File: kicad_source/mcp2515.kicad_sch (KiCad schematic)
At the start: 14 parts, among them CN4 SM04B-GHS-TB, CN5 SM04B-GHS-TB, U8 MCP2515T-I/SO, U9 SN65HVD232, Y1 X322516MLB4SI

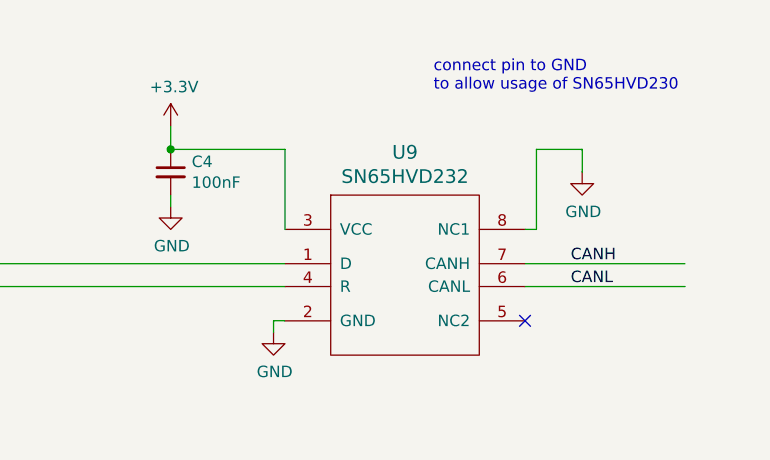
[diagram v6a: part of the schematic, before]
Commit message: switched to JLCPCB basic parts where possible
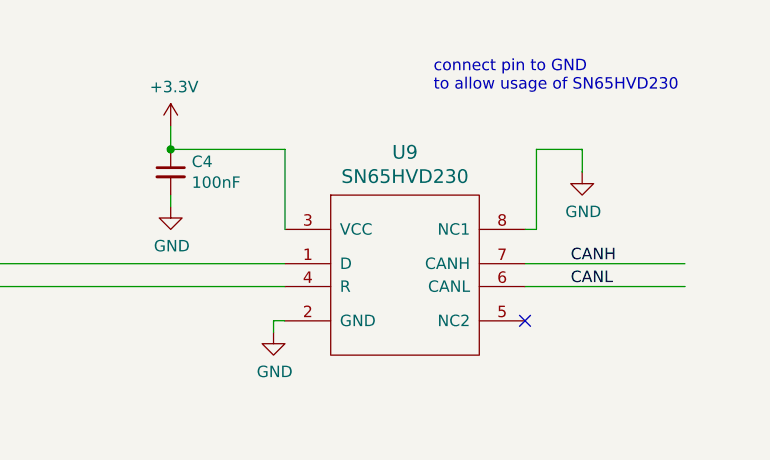
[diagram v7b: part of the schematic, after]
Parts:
- C3, C4: LCSC C314282 -> C14663
- C7, C8: LCSC C91367 -> C1634
- R1, R2, R3: LCSC C3152123 -> C25804
- U9: value SN65HVD232 -> SN65HVD230; LCSC C30530 -> C12084
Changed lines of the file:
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@@
     )
     (property "Datasheet" "" (id 3) (at 162.56 46.99 0))
-    (property "LCSC" "C314282" (id 4) (at 162.56 46.99 0)
+    (property "LCSC" "C14663" (id 4) (at 162.56 46.99 0)
       (effects (font (size 1.27 1.27)) hide)
     )
@@
     )
     (property "Datasheet" "" (id 3) (at 87.63 38.1 0))
-    (property "LCSC" "C3152123" (id 4) (at 87.63 38.1 0)
+    (property "LCSC" "C25804" (id 4) (at 87.63 38.1 0)
       (effects (font (size 1.27 1.27)) hide)
     )
@@
     )
     (property "Datasheet" "" (id 3) (at 80.01 38.1 0))
-    (property "LCSC" "C3152123" (id 4) (at 80.01 38.1 0)
+    (property "LCSC" "C25804" (id 4) (at 80.01 38.1 0)
       (effects (font (size 1.27 1.27)) hide)
     )
@@
     )
     (property "Datasheet" "" (id 3) (at 72.39 38.1 0))
-    (property "LCSC" "C3152123" (id 4) (at 72.39 38.1 0)
+    (property "LCSC" "C25804" (id 4) (at 72.39 38.1 0)
       (effects (font (size 1.27 1.27)) hide)
     )
@@
       (effects (font (size 1.524 1.524)))
     )
-    (property "Value" "SN65HVD232" (id 1) (at 224.155 46.2026 0)
+    (property "Value" "SN65HVD230" (id 1) (at 224.155 46.2026 0)
       (effects (font (size 1.524 1.524)))
     )
@@
       (effects (font (size 1.524 1.524)))
     )
-    (property "LCSC" "C30530" (id 4) (at 210.82 66.04 0)
+    (property "LCSC" "C12084" (id 4) (at 210.82 66.04 0)
       (effects (font (size 1.27 1.27)) hide)
     )
@@
     )
     (property "Datasheet" "" (id 3) (at 198.12 45.72 0))
-    (property "LCSC" "C314282" (id 4) (at 198.12 45.72 0)
+    (property "LCSC" "C14663" (id 4) (at 198.12 45.72 0)
       (effects (font (size 1.27 1.27)) hide)
     )
@@
     )
     (property "Datasheet" "" (id 3) (at 176.53 85.09 0))
-    (property "LCSC" "C91367" (id 4) (at 176.53 85.09 0)
+    (property "LCSC" "C1634" (id 4) (at 176.53 85.09 0)
       (effects (font (size 1.27 1.27)) hide)
     )
@@
     )
     (property "Datasheet" "" (id 3) (at 163.83 85.09 0))
-    (property "LCSC" "C91367" (id 4) (at 163.83 85.09 0)
-      (effects (font (size 1.27 1.27)) hide)
-    )
+    (property "LCSC" "C1634" (id 4) (at 163.83 85.09 0)
+      (effects (font (size 1.27 1.27)) hide)
+    )
